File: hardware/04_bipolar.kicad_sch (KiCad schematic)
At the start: 25 parts, among them U4 TPS65131RGER

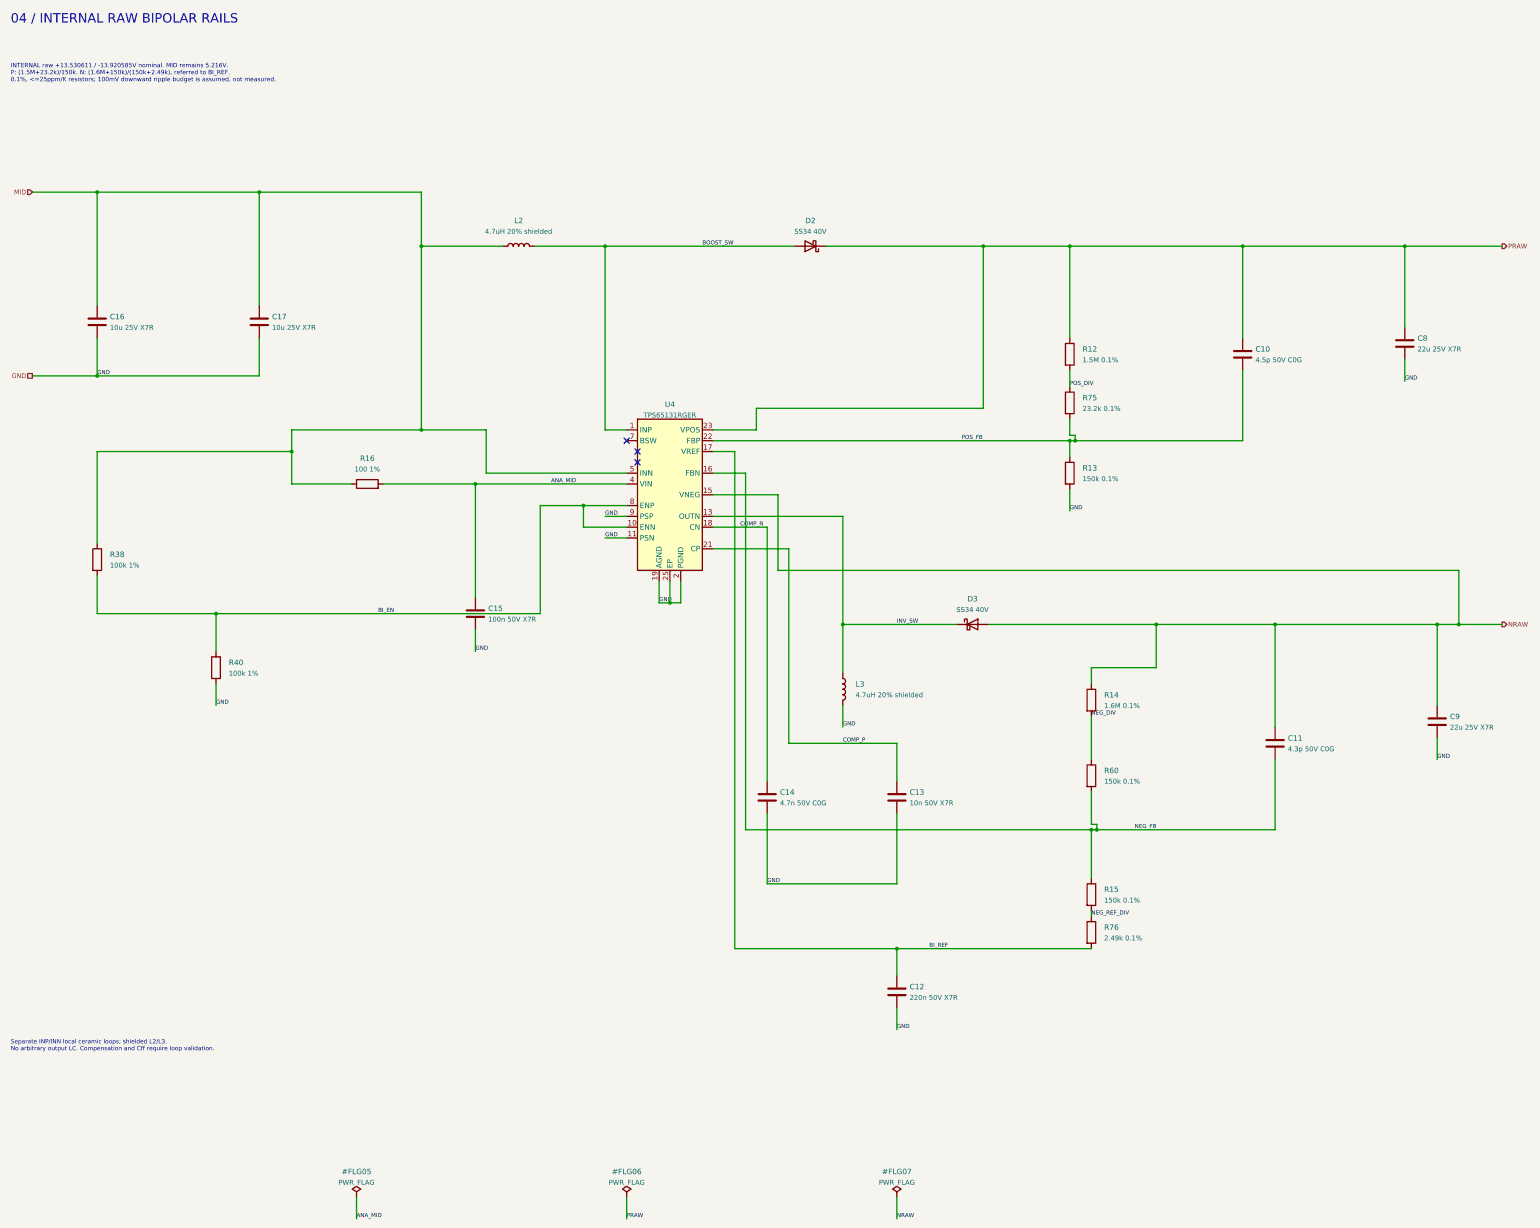
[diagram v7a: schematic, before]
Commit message: Apply Basic passive substitutions with corrected dividers, 1206 capacitor routing and verified prototype release
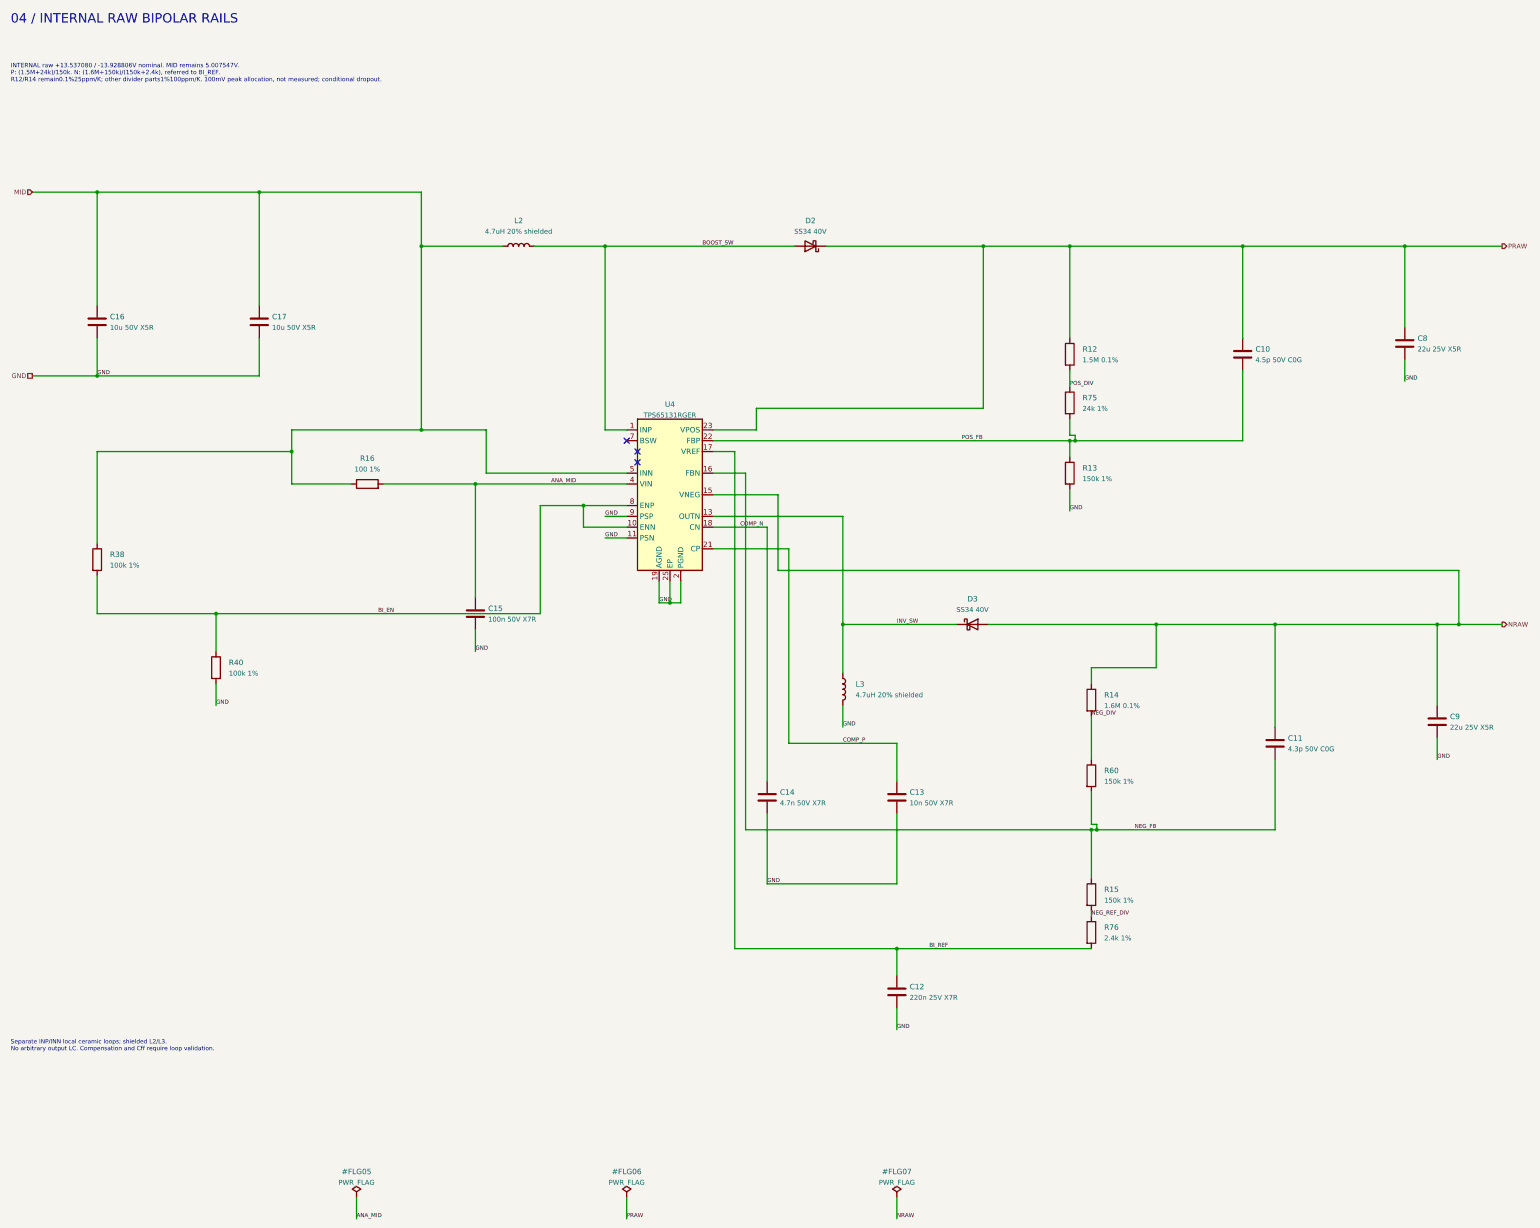
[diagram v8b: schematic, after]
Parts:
- C12: value 220n 50V X7R -> 220n 25V X7R; LCSC C107083 -> C21120; MPN CC0603KRX7R9BB224 -> CL10B224KA8NNNC; Manufacturer YAGEO -> Samsung Electro-Mechanics; NOTE Effective capacitance under DC bias and temperature must be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 -> CL10B224KA8NNNC,220n +/-10%,25V X7R0603. BI_REF1.2..1.225V;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
- C14: value 4.7n 50V C0G -> 4.7n 50V X7R; LCSC C576818 -> C53987; MPN CC0603JRNPO9BN472 -> 0603B472K500NT; Manufacturer YAGEO -> FH (Guangdong Fenghua Advanced Tech); NOTE YAGEO CC0603JRNPO9BN472: 4.7nF +/-5%, 50V NP0. TI recommend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 -> FH0603B472K500NT:4.7n +/-10%,50V X7R0603. Authorized CN err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
- C16, C17: value 10u 25V X7R -> 10u 50V X5R; LCSC C14860 -> C13585; MPN CL31B106KAHNNNE -> CL31A106KBHNNNE
- C8, C9: value 22u 25V X7R -> 22u 25V X5R; footprint BigModular:C_1210_3225Metric -> BigModular:C_1206_3216Metric; LCSC C53084530 -> C12891; MPN CC1210X7R25V226MN -> CL31A226KAHNNNE; Manufacturer (none) -> Samsung Electro-Mechanics
- R12, R14: NOTE Approved raw +13.530611/-13.920585V: 0.1%, <=25ppm/K. R12+R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 -> Retained exact precision upper resistor; 0.1%,25ppm/K. Raw 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
- R13, R15, R60: value 150k 0.1% -> 150k 1%; LCSC C326734 -> C22807; MPN RT0603BRD07150KL -> 0603WAF1503T5E; Manufacturer YAGEO -> UNI-ROYAL(Uniroyal Elec); NOTE Approved raw +13.530611/-13.920585V: 0.1%, <=25ppm/K. R12+R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 -> Authorized Basic1%,100ppm/K substitution. Raw nominal+13.53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
- R75: value 23.2k 0.1% -> 24k 1%; LCSC C861244 -> C23352; MPN RT0603BRD0723K2L -> 0603WAF2402T5E; Manufacturer Yageo -> UNI-ROYAL(Uniroyal Elec); NOTE Approved raw +13.530611/-13.920585V: 0.1%, <=25ppm/K. R12+R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 -> Authorized Basic1%,100ppm/K substitution. Raw nominal+13.53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
- R76: value 2.49k 0.1% -> 2.4k 1%; LCSC C861299 -> C22940; MPN RT0603BRD072K49L -> 0603WAF2401T5E; Manufacturer Yageo -> UNI-ROYAL(Uniroyal Elec); NOTE Approved raw +13.530611/-13.920585V: 0.1%, <=25ppm/K. R12+R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 -> Authorized Basic1%,100ppm/K substitution. Raw nominal+13.53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
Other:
- note added: "INTERNAL raw +13.537080 / -13.928806V nominal. MID remains 5.007547V. P: (1.5M+24k)/150k. N: (1.6M+150k)/(150k+2.4k), referred to BI_REF. R12/R14 remain0.1%25ppm/K; other divider parts1%100ppm/K. 100mV peak allocation, not measured; conditional dropout."
- note removed: "INTERNAL raw +13.530611 / -13.920585V nominal. MID remains 5.216V. P: (1.5M+23.2k)/150k. N: (1.6M+150k)/(150k+2.49k), referred to BI_REF. 0.1%, <=25ppm/K resistors; 100mV downward ripple budget is assumed, not measured."
